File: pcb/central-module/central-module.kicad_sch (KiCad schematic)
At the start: 16 parts, among them J1 Conn_01x10_Pin, J2 Screw_Terminal_01x04, J3 Conn_01x04_Pin, J4 Screw_Terminal_01x03, J6 Screw_Terminal_01x05, U1 ESP32_DEVCITV1, U2 74HC245

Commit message: checks and gerber
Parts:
- removed J6: Screw_Terminal_01x05, symbol Connector:Screw_Terminal_01x05
- added C3: 100n, Capacitor_THT:C_Disc_D4.3mm_W1.9mm_P5.00mm, symbol Device:C
- added J5: Screw_Terminal_01x04, TerminalBlock_MetzConnect:TerminalBlock_MetzConnect_Type011_RT05504HBWC_1x04_P5.00mm_Horizontal, symbol Connector:Screw_Terminal_01x04
- C1, C2: footprint (none) -> Capacitor_THT:C_Disc_D4.3mm_W1.9mm_P5.00mm
- F1, F2, F3, F4: footprint (none) -> Fuse:Fuseholder_Littelfuse_445_030_series_5x20mm
- J1: footprint (none) -> JS_Local:TE_CON_5499922-1_BIGGERHULL
- J2: footprint (none) -> TerminalBlock_MetzConnect:TerminalBlock_MetzConnect_Type011_RT05504HBWC_1x04_P5.00mm_Horizontal
- J3: footprint (none) -> Connector_JST:JST_VH_B4PS-VH_1x04_P3.96mm_Horizontal
- J4: footprint (none) -> TerminalBlock_MetzConnect:TerminalBlock_MetzConnect_Type011_RT05503HBWC_1x03_P5.00mm_Horizontal
- R1, R2: footprint (none) -> Resistor_THT:R_Axial_DIN0207_L6.3mm_D2.5mm_P10.16mm_Horizontal
- RV1: footprint (none) -> Varistor:RV_Disc_D9mm_W3.3mm_P5mm
- U1: footprint (none) -> JS_Local:ESP32_DEVKITV1
- U2: footprint (none) -> Package_DIP:DIP-20_W7.62mm
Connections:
- net +24V: no longer F3.1, J4.3 (Pin_3)
- net +5V: now also C3.1
- net GND: now also C3.2
- net N: now also J5.2 (Pin_2), J5.4 (Pin_4)
- net P: now also J5.1 (Pin_1)
- net P_FUSED: now reaches F1.1
- net P_FUSED: now also J5.3 (Pin_3)
- new net: F3.1, J4.3 (Pin_3)
- no-connect marks 4 -> 24
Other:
- moved on the sheet: F1, RV1

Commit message: improvements first soldering
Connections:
- net 24VAC_P_UF: now reaches F2.1, J2.4 (Pin_4)
- net +24V_UF: now reaches F3.1, J4.3 (Pin_3)
- net T_BRIDGE: now reaches J2.2 (Pin_2), J2.3 (Pin_3)
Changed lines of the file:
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@@
+		)
+	)
+	(label "24VAC_P_UF"
+		(at 73.66 29.21 0)
+		(fields_autoplaced yes)
+		(effects
+			(font
+				(size 1.27 1.27)
+			)
+			(justify left bottom)
+		)
+	)
+	(label "T_BRIDGE"
+		(at 71.12 31.75 0)
+		(fields_autoplaced yes)
+		(effects
+			(font
+				(size 1.27 1.27)
+			)
+			(justify left bottom)
 		)
 	)
@@
 		(fields_autoplaced yes)
 		(effects
+			(font
+				(size 1.27 1.27)
+			)
+			(justify left bottom)
+		)
+	)
+	(label "+24V_UF"
+		(at 71.12 46.99 0)
+		(fields_autoplaced yes)
+		(effects

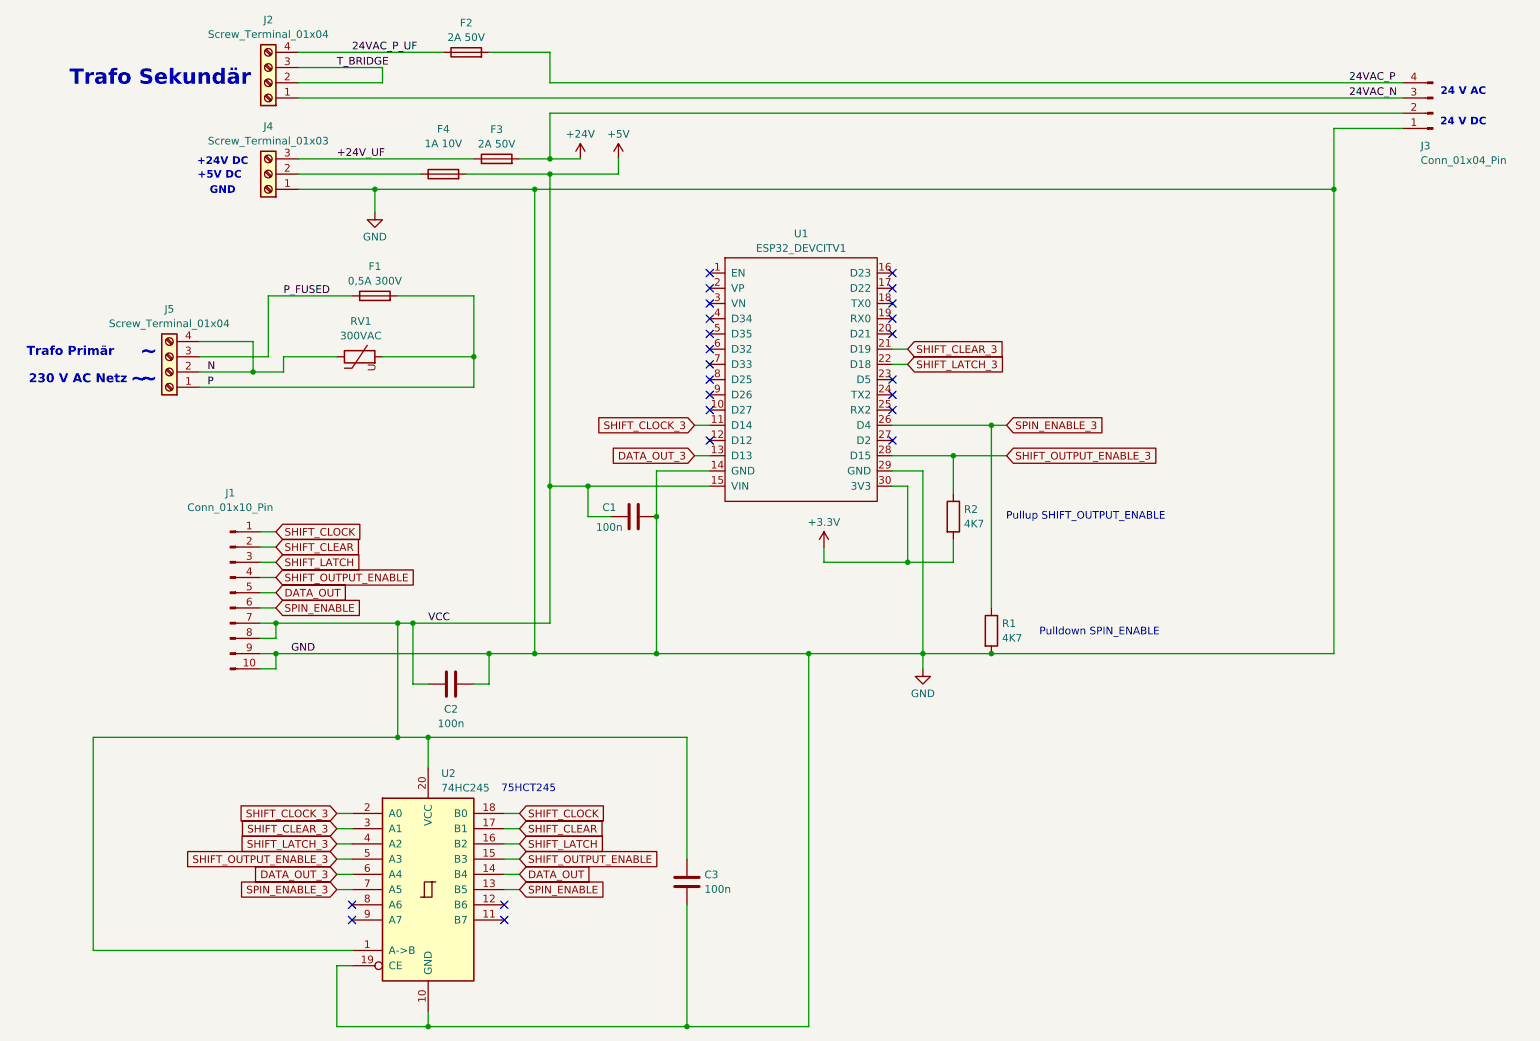
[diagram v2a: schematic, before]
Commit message: dc power fet
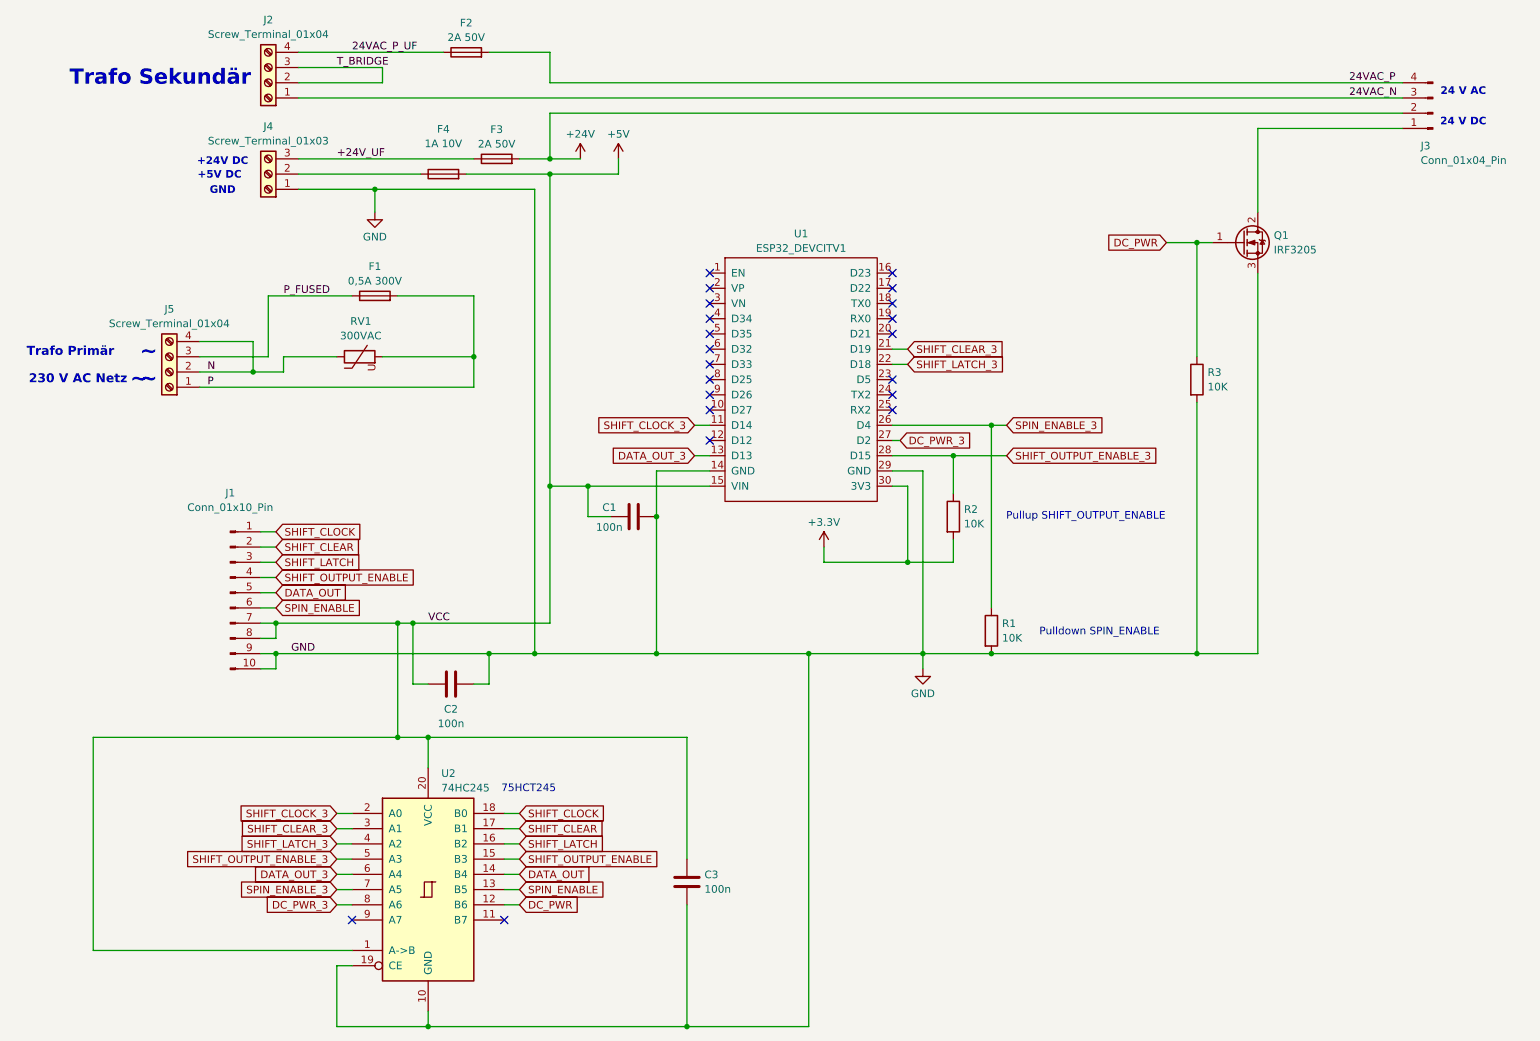
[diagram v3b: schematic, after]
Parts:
- added Q1: IRF3205, Package_TO_SOT_THT:TO-220-3_Vertical, symbol Transistor_FET:IRF3205
- added R3: 10K, Resistor_THT:R_Axial_DIN0207_L6.3mm_D2.5mm_P10.16mm_Horizontal, symbol Device:R
- R1, R2: value 4K7 -> 10K
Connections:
- net GND: now also Q1.3 (S), R3.2; no longer J3.1 (Pin_1)
- net DC_PWR_3: now reaches U1.27 (D2)
- net DC_PWR_3: now also U2.8 (A6)
- net DC_PWR: now reaches U2.12 (B6)
- net DC_PWR: now also Q1.1 (G), R3.1
- new net: J3.1 (Pin_1), Q1.2 (D)
- no-connect marks 24 -> 21

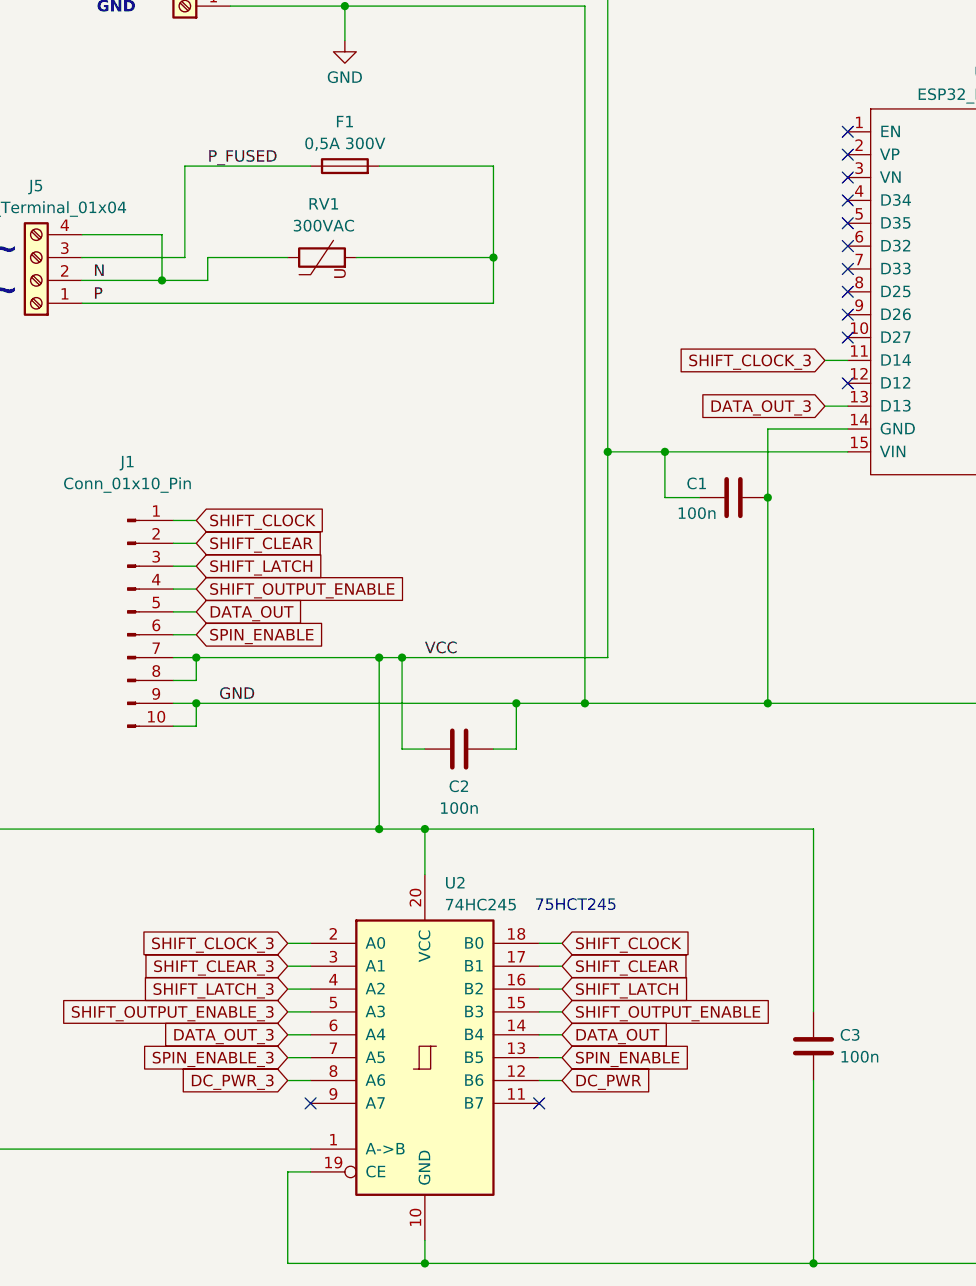
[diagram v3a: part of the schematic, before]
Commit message: unused pins, varistor
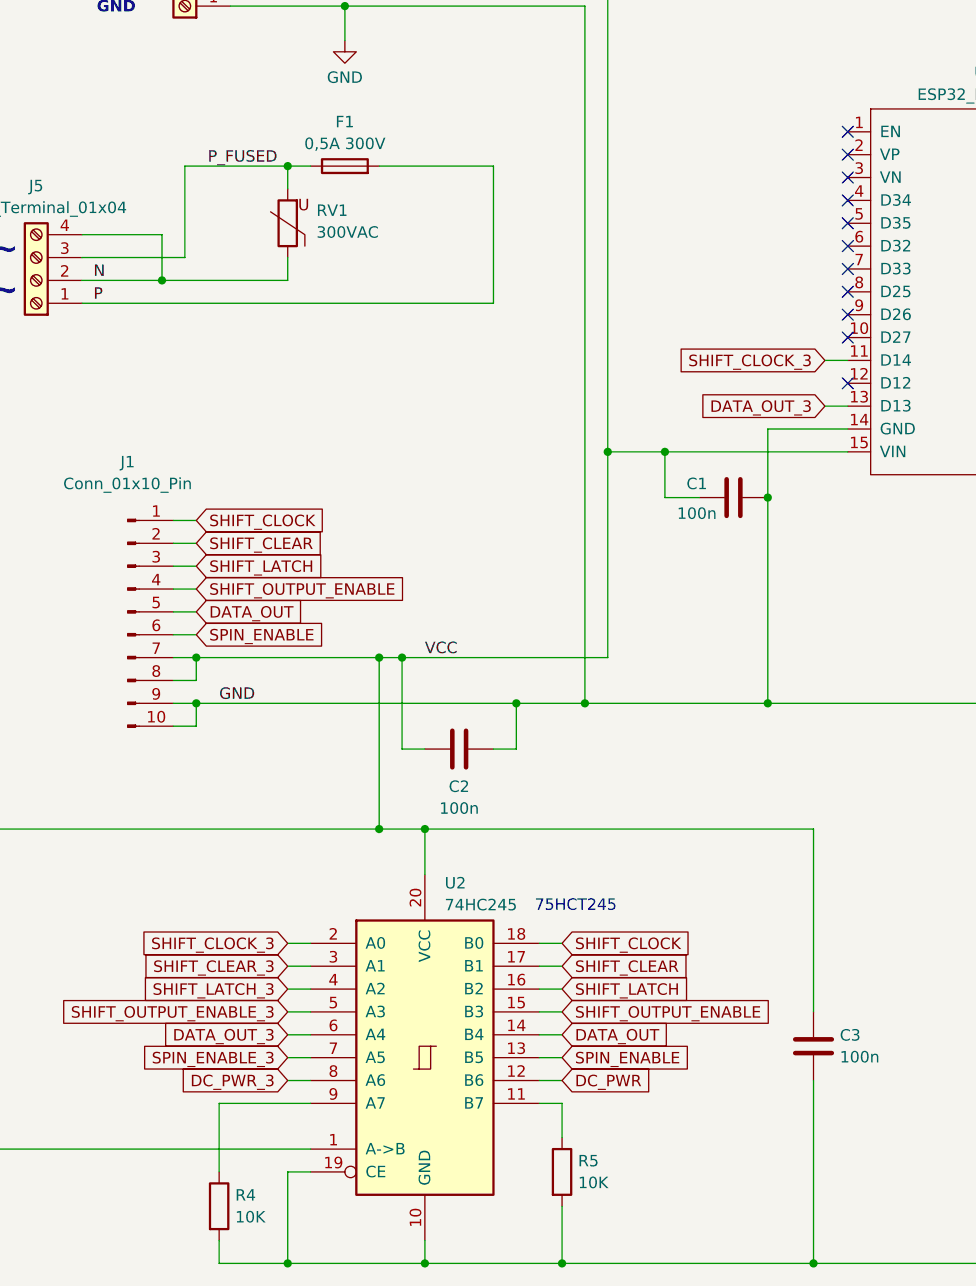
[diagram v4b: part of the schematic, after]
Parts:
- added R4, R5: 10K, symbol Device:R
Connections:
- net GND: now also R4.2, R5.2
- net P: no longer RV1.2
- net P_FUSED: now also RV1.2
- net at U2.11 (B7): now also R5.1
- net at U2.9 (A7): now also R4.1
- no-connect marks 21 -> 19
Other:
- moved on the sheet: RV1

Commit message: many improvements
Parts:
- R4, R5: footprint (none) -> Resistor_THT:R_Axial_DIN0207_L6.3mm_D2.5mm_P10.16mm_Horizontal
- RV1: footprint Varistor:RV_Disc_D9mm_W3.3mm_P5mm -> Varistor:RV_Disc_D15.5mm_W3.9mm_P7.5mm
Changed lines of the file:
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@@
 			)
 		)
-		(property "Footprint" ""
+		(property "Footprint" "Resistor_THT:R_Axial_DIN0207_L6.3mm_D2.5mm_P10.16mm_Horizontal"
 			(at 61.722 185.42 90)
 			(effects
@@
 			)
 		)
-		(property "Footprint" ""
+		(property "Footprint" "Resistor_THT:R_Axial_DIN0207_L6.3mm_D2.5mm_P10.16mm_Horizontal"
 			(at 99.822 181.61 90)
 			(effects
@@
 			)
 		)
-		(property "Footprint" "Varistor:RV_Disc_D9mm_W3.3mm_P5mm"
+		(property "Footprint" "Varistor:RV_Disc_D15.5mm_W3.9mm_P7.5mm"
 			(at 72.898 76.2 90)
 			(effects

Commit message: graytable, both pcbs
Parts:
- added R6: 4K7, Resistor_THT:R_Axial_DIN0207_L6.3mm_D2.5mm_P10.16mm_Horizontal, symbol Device:R
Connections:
- net DC_PWR: now also R6.1; no longer Q1.1 (G)
- new net: Q1.1 (G), R6.2
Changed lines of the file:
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@@
-	)
-	(junction
-		(at 214.63 60.96)
-		(diameter 0)
-		(color 0 0 0 0)
 	)
 	(junction
@@
 	)
 	(junction
+		(at 195.58 60.96)
+		(diameter 0)
+		(color 0 0 0 0)
+	)
+	(junction
 		(at 86.36 143.51)
 		(diameter 0)
@@
 	(wire
 		(pts
+			(xy 195.58 74.93) (xy 214.63 74.93)
+		)
+		(stroke
+			(width 0)
+			(type default)
+		)
+	)
+	(wire
+		(pts
 			(xy 101.6 191.77) (xy 129.54 191.77)
 		)
@@
 	(wire
 		(pts
+			(xy 209.55 60.96) (xy 217.17 60.96)
+		)
+		(stroke
+			(width 0)
+			(type default)
+		)
+	)
+	(wire
+		(pts
 			(xy 83.82 124.46) (xy 106.68 124.46)
 		)
@@
 	(wire
 		(pts
-			(xy 209.55 60.96) (xy 214.63 60.96)
-		)
-		(stroke
-			(width 0)
-			(type default)
-		)
-	)
-	(wire
-		(pts
 			(xy 63.5 173.99) (xy 73.66 173.99)
 		)
@@
 	(wire
 		(pts
+			(xy 214.63 74.93) (xy 214.63 80.01)
+		)
+		(stroke
+			(width 0)
+			(type default)
+		)
+	)
+	(wire
+		(pts
 			(xy 101.6 46.99) (xy 106.68 46.99)
 		)
@@
 	(wire
 		(pts
-			(xy 214.63 60.96) (xy 214.63 80.01)
+			(xy 195.58 60.96) (xy 195.58 74.93)
 		)
 		(stroke
@@
 	(wire
 		(pts
-			(xy 214.63 60.96) (xy 217.17 60.96)
-		)
-		(stroke
-			(width 0)
-			(type default)
-		)
-	)
-	(wire
-		(pts
 			(xy 58.42 114.3) (xy 60.96 114.3)
 		)
@@
 	(wire
 		(pts
+			(xy 195.58 60.96) (xy 201.93 60.96)
+		)
+		(stroke
+			(width 0)
+			(type default)
+		)
+	)
+	(wire
+		(pts
 			(xy 104.14 129.54) (xy 124.46 129.54)
 		)
@@
 		(pts
 			(xy 124.46 106.68) (xy 124.46 129.54)
+		)
+		(stroke
+			(width 0)
+			(type default)
+		)
+	)
+	(wire
+		(pts
+			(xy 187.96 60.96) (xy 195.58 60.96)
 		)
 		(stroke
@@
 	(global_label "DC_PWR"
 		(shape input)
-		(at 209.55 60.96 180)
+		(at 187.96 60.96 180)
 		(fields_autoplaced yes)
 		(effects
@@
 		)
 		(property "Intersheetrefs" "${INTERSHEET_REFS}"
-			(at 199.0658 60.96 0)
+			(at 177.4758 60.96 0)
 			(effects
 				(font
@@
 					(unit 1)
 				)
+			)
+		)
+	)
+	(symbol
+		(lib_id "Device:R")
+		(at 205.74 60.96 90)
+		(unit 1)
+		(exclude_from_sim no)
+		(in_bom yes)
+		(on_board yes)
+		(dnp no)
+		(fields_autoplaced yes)
+		(property "Reference" "R6"
+			(at 205.74 55.7995 90)
+			(effects
+				(font
+					(size 1.27 1.27)
+				)
+			)
+		)
+		(property "Value" "4K7"
+			(at 205.74 58.2238 90)
+			(effects
+				(font
+					(size 1.27 1.27)
+				)
+			)
+		)
+		(property "Footprint" "Resistor_THT:R_Axial_DIN0207_L6.3mm_D2.5mm_P10.16mm_Horizontal"
+			(at 205.74 62.738 90)
+			(effects
+				(font
+					(size 1.27 1.27)
+				)
+				(hide yes)
+			)
+		)
+		(property "Datasheet" "~"
+			(at 205.74 60.96 0)
+			(effects
+				(font
+					(size 1.27 1.27)
+				)
+				(hide yes)
+			)
+		)
+		(property "Description" "Resistor"
+			(at 205.74 60.96 0)
+			(effects
+				(font
+					(size 1.27 1.27)
+				)
+				(hide yes)
+			)
+		)
+		(pin "2"
+		)
+		(pin "1"
+		)
+		(instances
+			(project ""
+				(path "/f90170a8-70f2-410a-87cc-d7ebba9a5121"
+					(reference "R6")
+					(unit 1)
+				)

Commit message: fuses
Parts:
- F1: value 0,5A 300V -> 1A 300V
- F2: value 2A 50V -> 5A 50V
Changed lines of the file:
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@@
 			)
 		)
-		(property "Value" "2A 50V"
+		(property "Value" "5A 50V"
 			(at 92.71 26.7278 90)
 			(effects
@@
 			)
 		)
-		(property "Value" "0,5A 300V"
+		(property "Value" "1A 300V"
 			(at 77.47 67.3678 90)
 			(effects

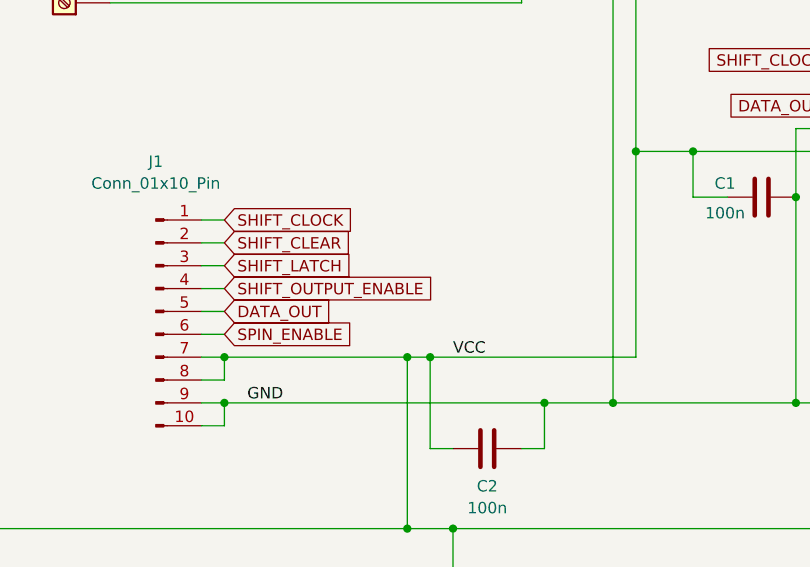
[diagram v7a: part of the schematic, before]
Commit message: 14 modules, central pcb serial termination
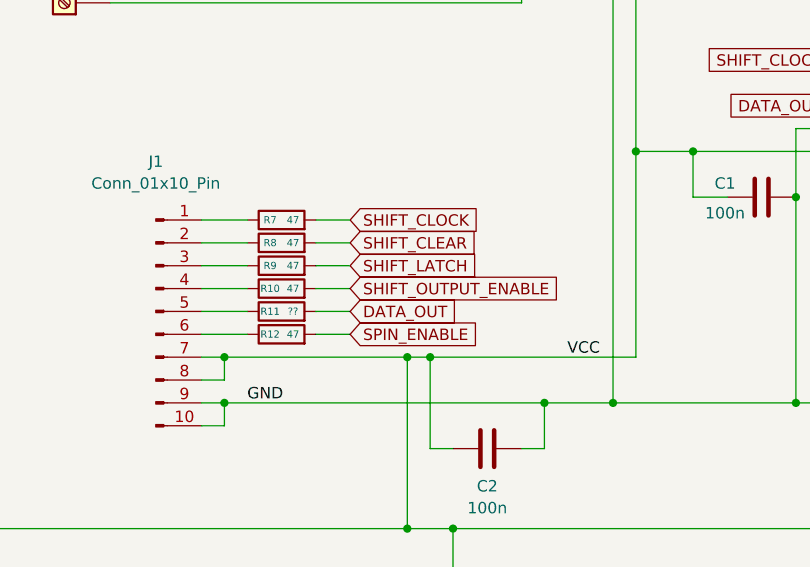
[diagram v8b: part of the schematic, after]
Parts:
- added R10, R12, R7, R8, R9: 47, Resistor_THT:R_Axial_DIN0207_L6.3mm_D2.5mm_P10.16mm_Horizontal, symbol Device:R
- added R11: ??, Resistor_THT:R_Axial_DIN0207_L6.3mm_D2.5mm_P10.16mm_Horizontal, symbol Device:R
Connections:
- net DATA_OUT: now also R11.2; no longer J1.5 (Pin_5)
- net SHIFT_CLEAR: now also R8.2; no longer J1.2 (Pin_2)
- net SHIFT_CLOCK: now also R7.2; no longer J1.1 (Pin_1)
- net SHIFT_LATCH: now also R9.2; no longer J1.3 (Pin_3)
- net SHIFT_OUTPUT_ENABLE: now also R10.2; no longer J1.4 (Pin_4)
- net SPIN_ENABLE: now also R12.2; no longer J1.6 (Pin_6)
- new net: J1.3 (Pin_3), R9.1
- new net: J1.6 (Pin_6), R12.1
- new net: J1.1 (Pin_1), R7.1
- new net: J1.4 (Pin_4), R10.1
- new net: J1.5 (Pin_5), R11.1
- new net: J1.2 (Pin_2), R8.1
